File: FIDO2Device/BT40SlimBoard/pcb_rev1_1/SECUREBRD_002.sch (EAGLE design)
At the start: 31 parts, among them CN1 2137160001, CN2 IF_5PIN_H, CN3 IF_2PIN_SOL, SW1 SKRPACE010, SW2 SKRPACE010, SW3 SKTADAE010, U1 BT40, U2 ADP122ACPZ-3.3-R7

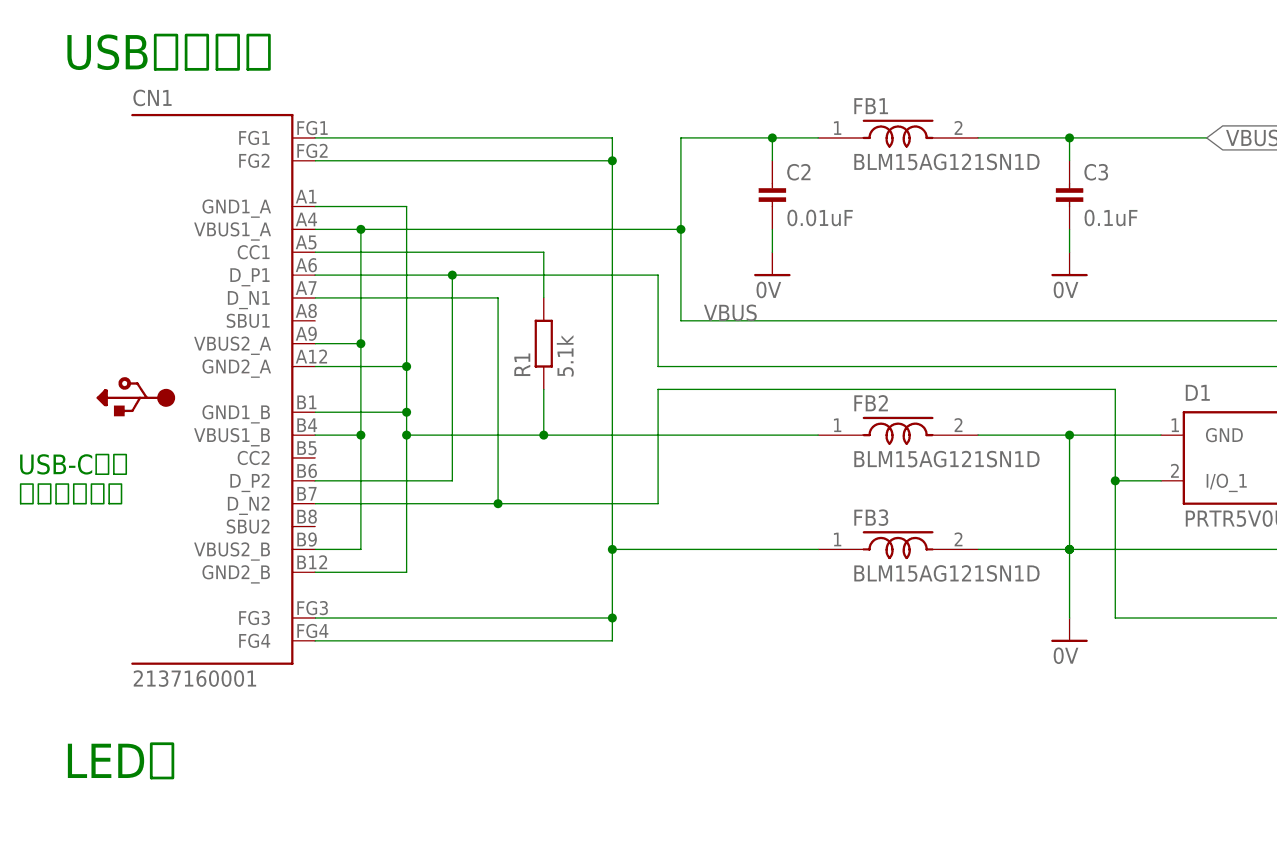
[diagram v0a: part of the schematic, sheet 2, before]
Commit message: 回路図を更新
・USB-Cプラグ部品を`USB4105-GF-A`に更新
（前回試作失敗の原因となった部品`2137160001`から差し替え）
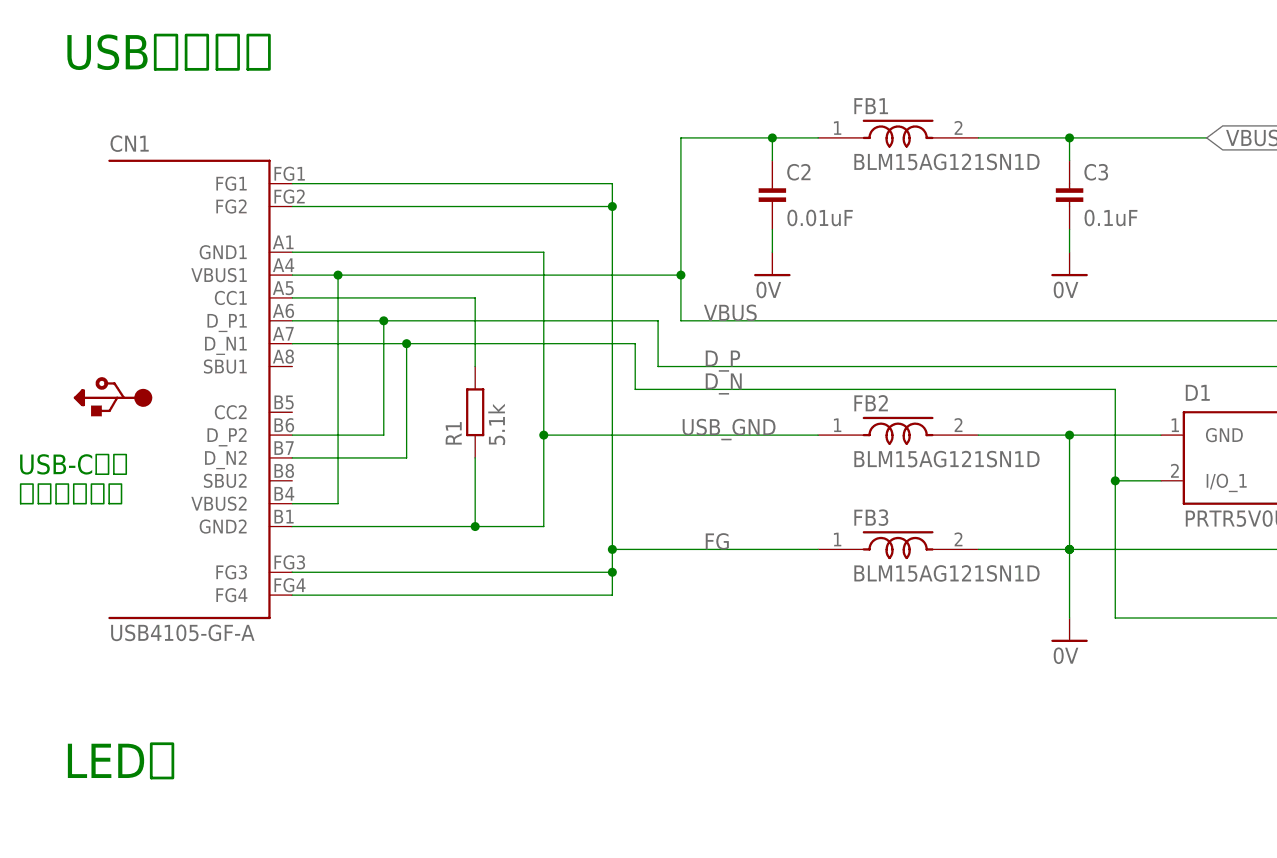
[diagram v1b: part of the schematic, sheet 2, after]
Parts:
- CN1: value 2137160001 -> USB4105-GF-A; device Connectors:2137160001 -> Connectors:USB4105-GF-A
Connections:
- net USB_GND: now also CN1.GND1, CN1.GND2; no longer CN1.GND1_A, CN1.GND1_B, CN1.GND2_A, CN1.GND2_B
- net VBUS: now also CN1.VBUS1, CN1.VBUS2; no longer CN1.VBUS1_A, CN1.VBUS1_B, CN1.VBUS2_A, CN1.VBUS2_B
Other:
- moved on the sheet: R1

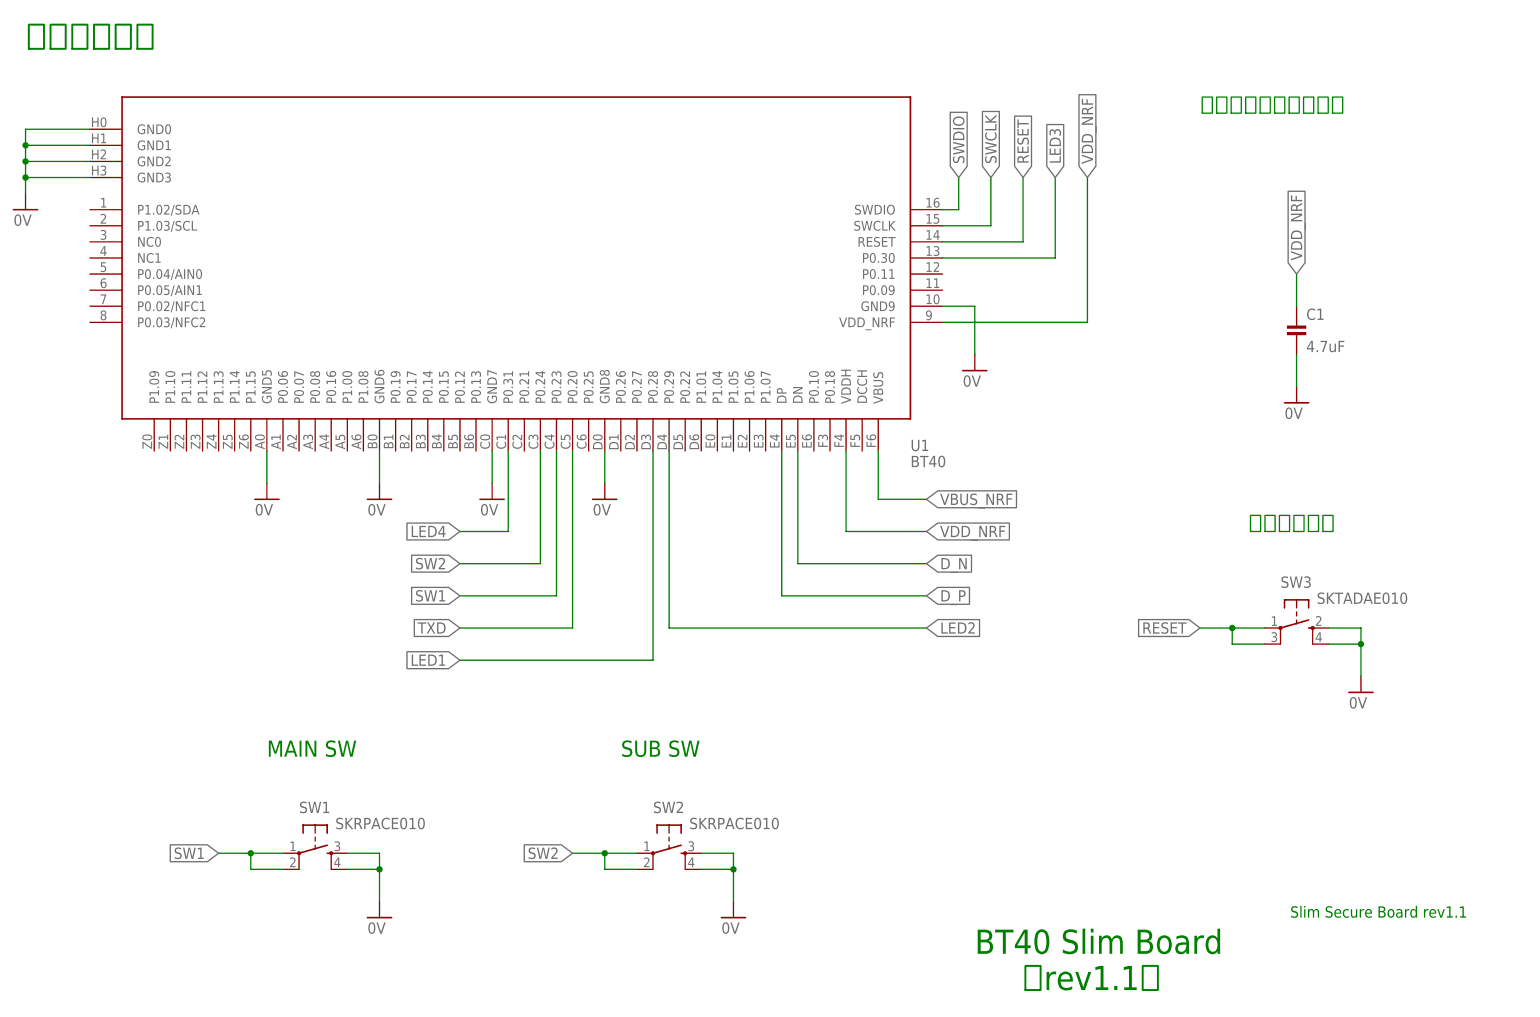
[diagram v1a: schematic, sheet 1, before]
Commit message: 回路図を修正
・２番目のスイッチを撤去
・リアルタイムクロックモジュールおよび周辺部品を配置
・フェライトビーズの記号をFB-->Lに変更
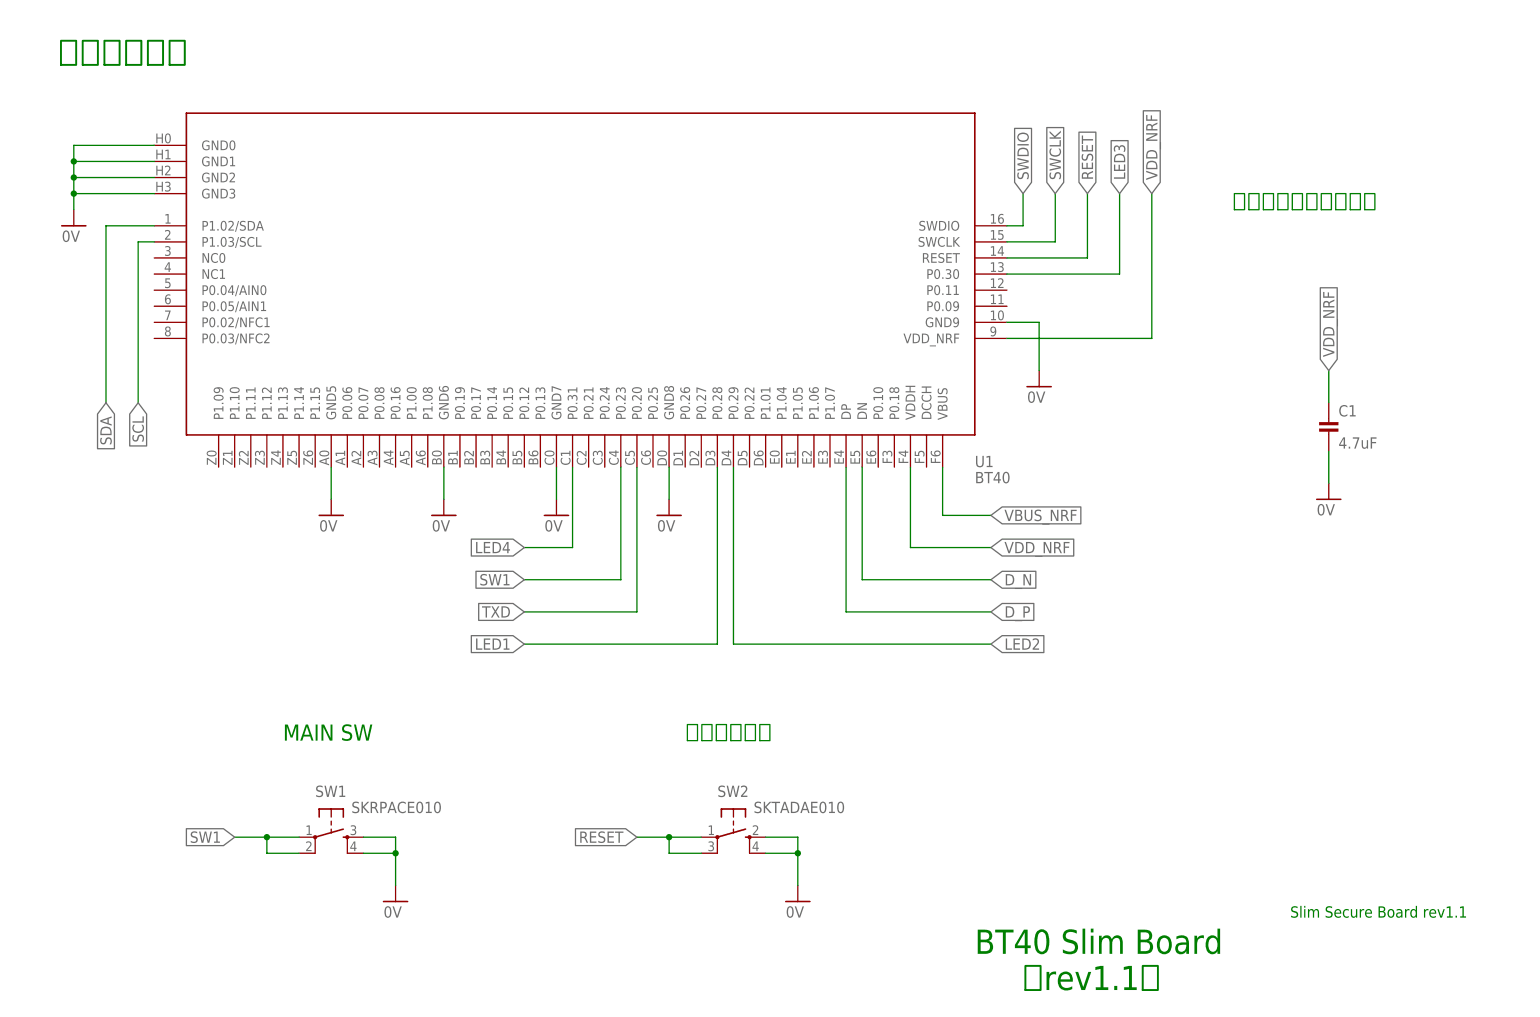
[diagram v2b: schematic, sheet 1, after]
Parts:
- removed SW3: SKTADAE010, Parts:SKTADAE010
- added C8, C9: 0.1uF, Parts:CAP_0402K
- added R6, R7, R8: 10k, Parts:RESISTOR_0402
- added R9: 390, Parts:RESISTOR_0402
- added U3: RV-3028-C7, ICs:RV-3028-C7
- SW2: value SKRPACE010 -> SKTADAE010; device Parts:SKRPACE010 -> Parts:SKTADAE010
- renumbered FB1 to L1, FB2 to L2, FB3 to L3
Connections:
- removed net N$5: BAT1.+, D3.A
- removed net SW2: SW2.P, SW2.P1, U1.P0.24
- new net N$4: R8.2, U3.EVI
- new net N$9: C9.1, R9.1, U3.VBACKUP
- new net SCL: R7.1, U1.P1.03/SCL, U3.SCL@
- new net SDA: R6.1, U1.P1.02/SDA, U3.SDA@
- new net VDD_BAT: BAT1.+, D3.A, R9.2
- net 0V: now also C8.2, C9.2, R8.1, U3.VSS; no longer SW3.S, SW3.S1
- net RESET: now also SW2.P, SW2.P1; no longer SW3.P, SW3.P1
- net VDD_NRF: now also C8.1, R6.2, R7.2, U3.VDD
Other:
- note added: "常時給電が必要なため、ボタン乾電池に接続します。"
- note added: "時刻同期部"
- note removed: "SUB SW"
- moved on the sheet: BAT1, C1, C6, C7, CN3, D2, D3, SW1, SW2, U1, U2

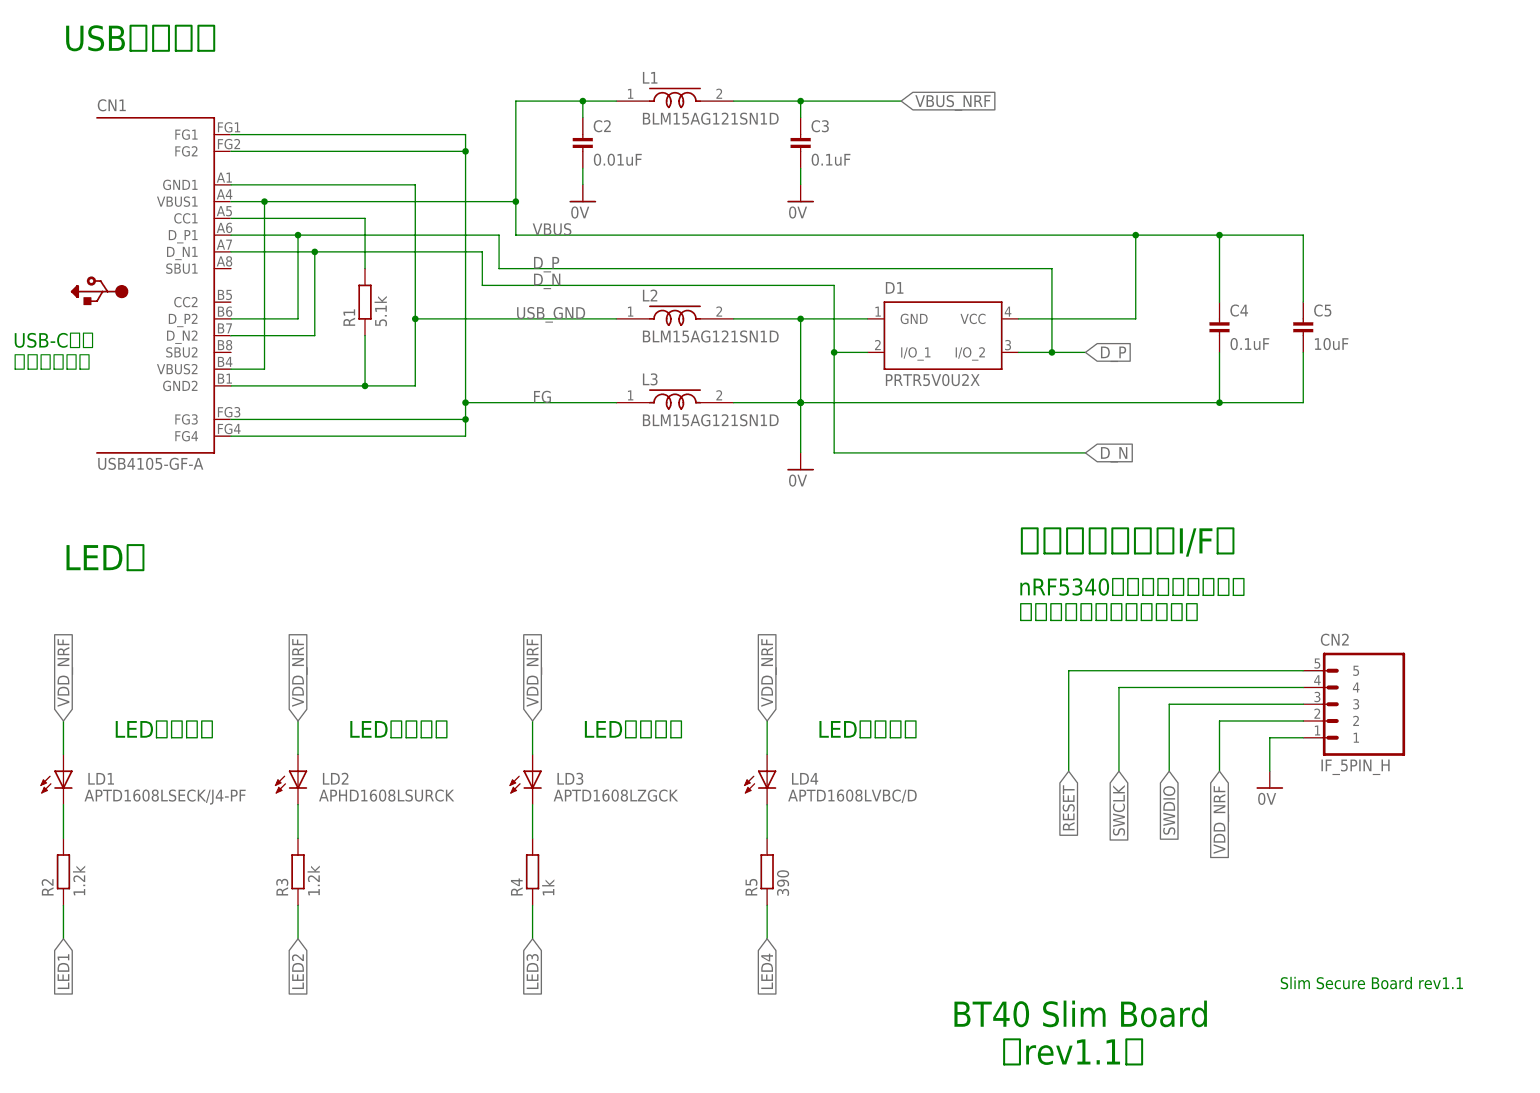
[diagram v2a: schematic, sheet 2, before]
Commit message: 回路図を修正
・TXDをプログラム用のスルーホール群に含めるよう修正
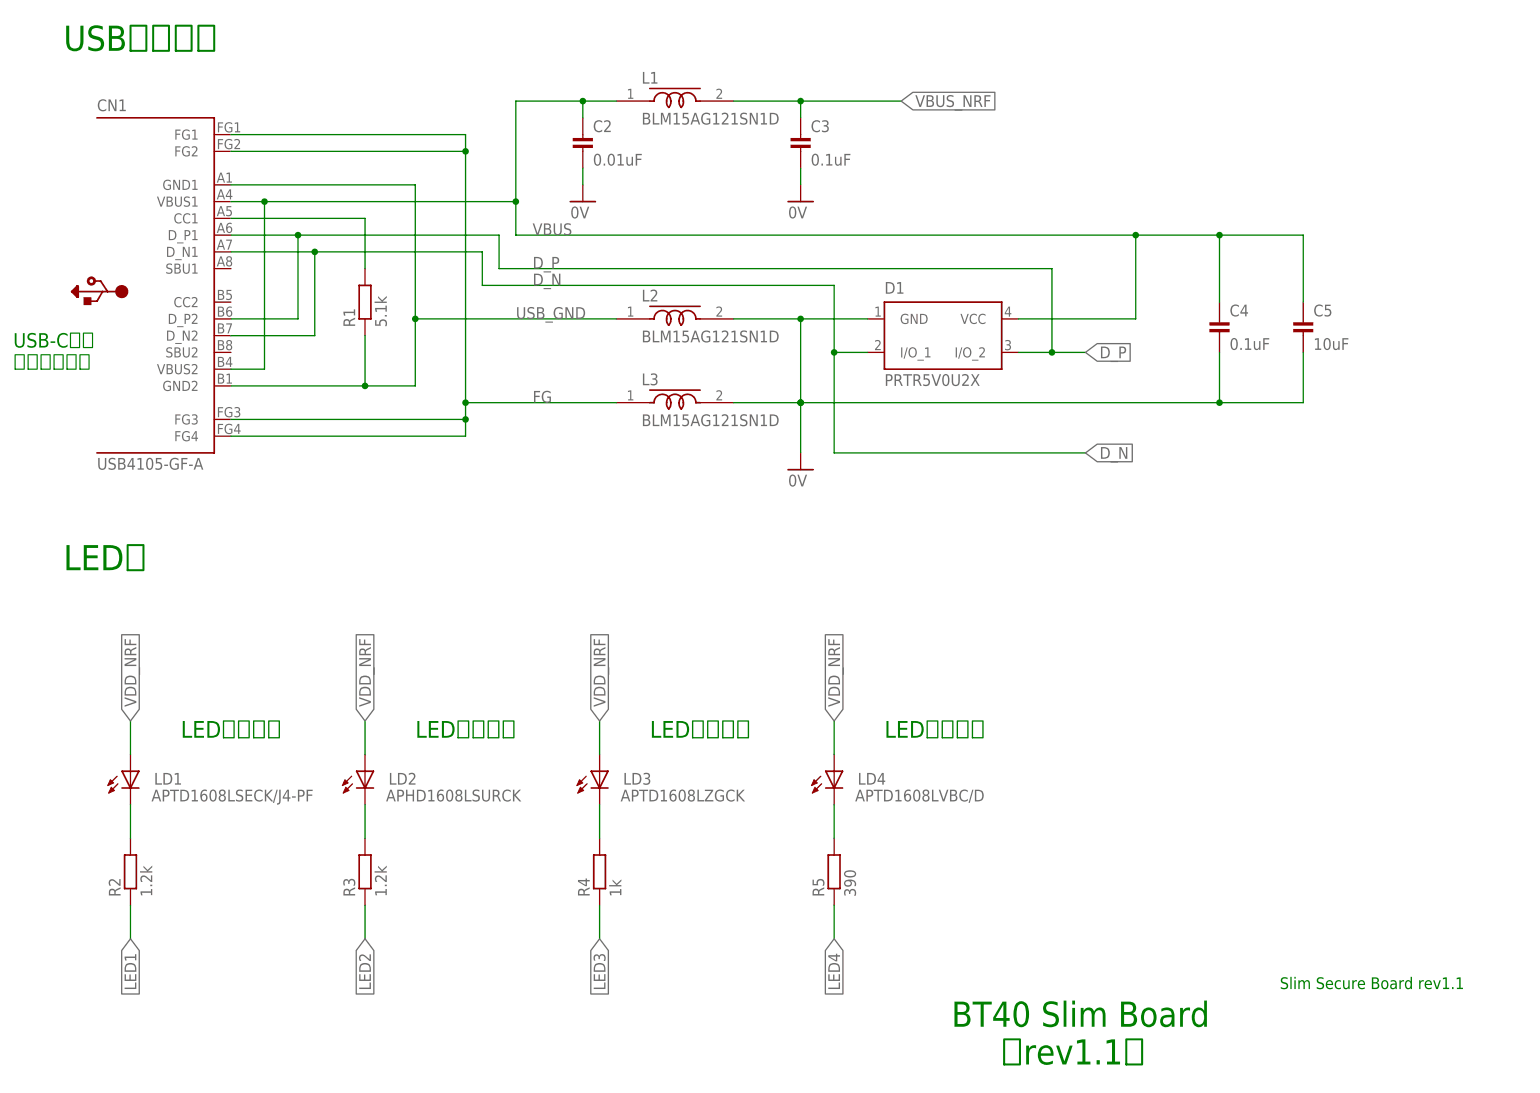
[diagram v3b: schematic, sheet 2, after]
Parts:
- removed CN2: IF_5PIN_H, Connectors:IF_5PIN_H
- CN3: value IF_2PIN_SOL -> IF_6PIN; device Connectors:IF_2PIN_SOL -> Connectors:IF_6PIN
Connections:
- net 0V: no longer CN2.1
- net RESET: now also CN3.5; no longer CN2.5
- net SWCLK: now also CN3.4; no longer CN2.4
- net SWDIO: now also CN3.3; no longer CN2.3
- net TXD: now also CN3.6; no longer CN3.2
- net VDD_NRF: now also CN3.2; no longer CN2.2
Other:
- note removed: "ユーティリティーI/F部"
- moved on the sheet: C1, LD1, LD2, LD3, LD4, R2, R3, R4, R5
